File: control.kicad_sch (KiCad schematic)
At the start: 8 parts, among them SW1 EC11, U1 Arduino_Nano, U2 Si5351A, U3 OLED_128x64

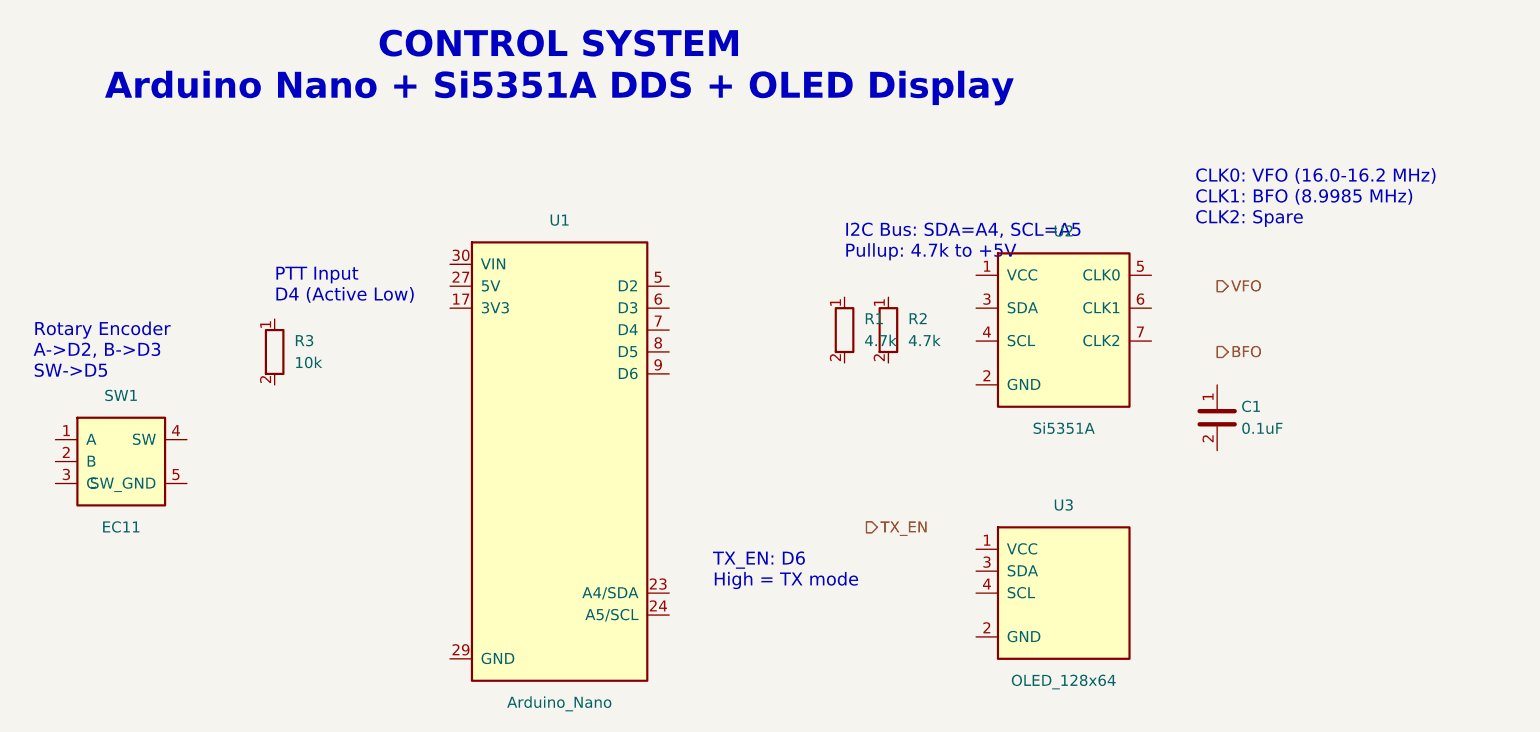
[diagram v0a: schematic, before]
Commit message: Add initial PCB layout with complete component placement
- Create 2-layer PCB (200x100mm) based on KiCad schematic import
- Place all components including Arduino Nano, Si5351, SA612 mixers, SSD1306 OLED
- Position audio amplifier (LM386), voltage regulators (7805/7808), crystal filters
- Add discrete components: resistors, capacitors, inductors, diodes, transistors
- Include connectors for power (DC jack), antenna, speaker, and microphone
- Update .gitignore to exclude fp-info-cache and backup directories
- Update schematic symbols for all circuit blocks (audio, BPF/LPF, control, IF filter, mixer/modulator, power amp, power supply)
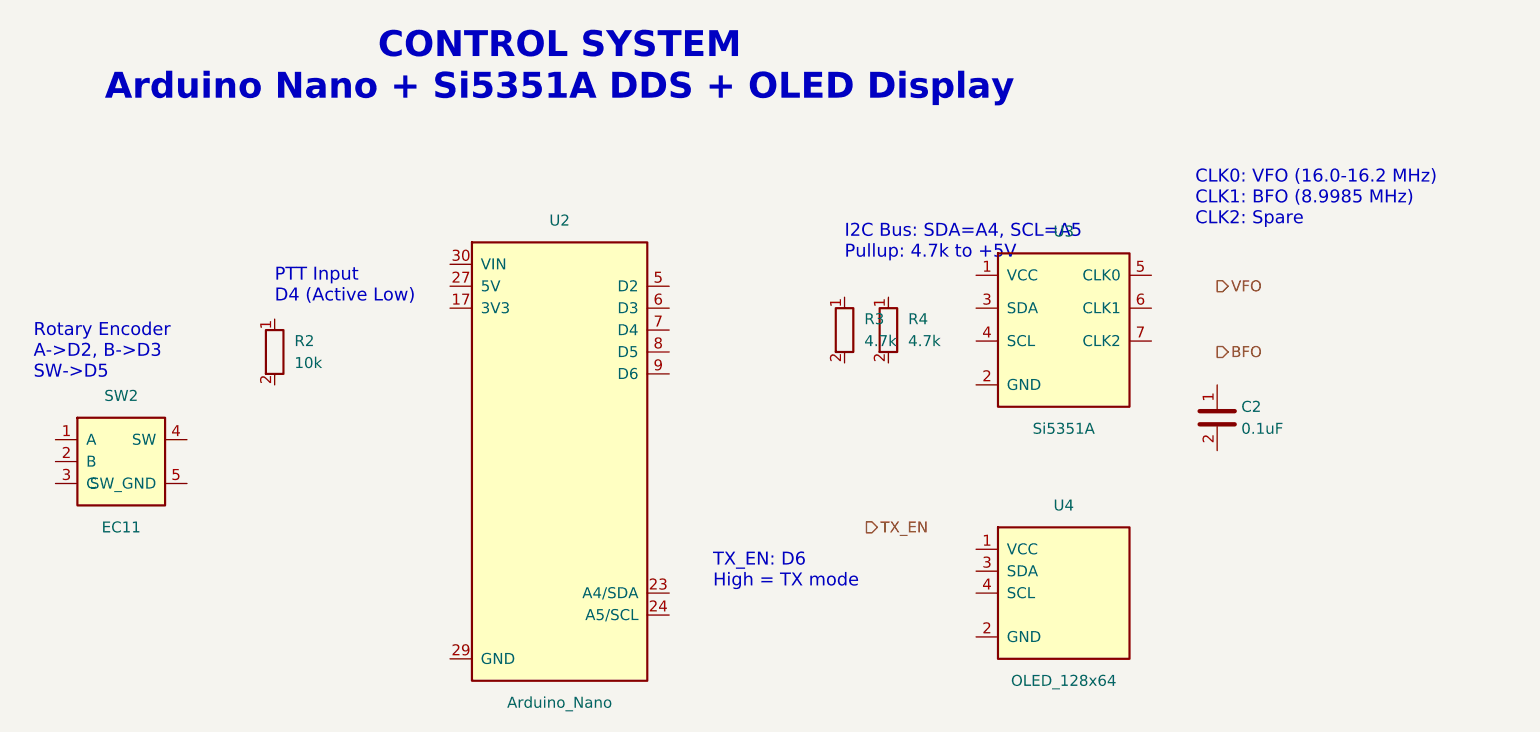
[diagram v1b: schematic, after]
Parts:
- removed C1: 0.1uF, symbol Device:C
- removed R1: 4.7k, symbol Device:R
- removed SW1: EC11, symbol Encoder:RotaryEncoder_SW
- removed U1: Arduino_Nano, symbol Arduino_Nano:Arduino_Nano
- removed U2: Si5351A, symbol Si5351:Si5351A_Module
- removed U3: OLED_128x64, symbol OLED:OLED_I2C_128x64
- added C2: 0.1uF, Capacitor_THT:CP_Radial_D5.0mm_P2.50mm, symbol Device:C
- added R4: 4.7k, Resistor_THT:R_Axial_DIN0207_L6.3mm_D2.5mm_P10.16mm_Horizontal, symbol Device:R
- added SW2: EC11, Connector_PinHeader_2.54mm:PinHeader_1x05_P2.54mm_Vertical, symbol Encoder:RotaryEncoder_SW
- added U2: Arduino_Nano, Module:Arduino_Nano, symbol Arduino_Nano:Arduino_Nano
- added U3: Si5351A, Connector_PinHeader_2.54mm:PinHeader_1x07_P2.54mm_Vertical, symbol Si5351:Si5351A_Module
- added U4: OLED_128x64, Connector_PinHeader_2.54mm:PinHeader_1x04_P2.54mm_Vertical, symbol OLED:OLED_I2C_128x64
- R2: value 4.7k -> 10k; footprint (none) -> Resistor_THT:R_Axial_DIN0207_L6.3mm_D2.5mm_P10.16mm_Horizontal
- R3: value 10k -> 4.7k; footprint (none) -> Resistor_THT:R_Axial_DIN0207_L6.3mm_D2.5mm_P10.16mm_Horizontal
